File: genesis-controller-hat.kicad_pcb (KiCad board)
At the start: 2 copper layers, 65 x 56 mm, 7 parts, among them J1 GPIO, J2 DSUB-9_Socket_Vertical_P2.77x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, J3 DSUB-9_Socket_Vertical_P2.77x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

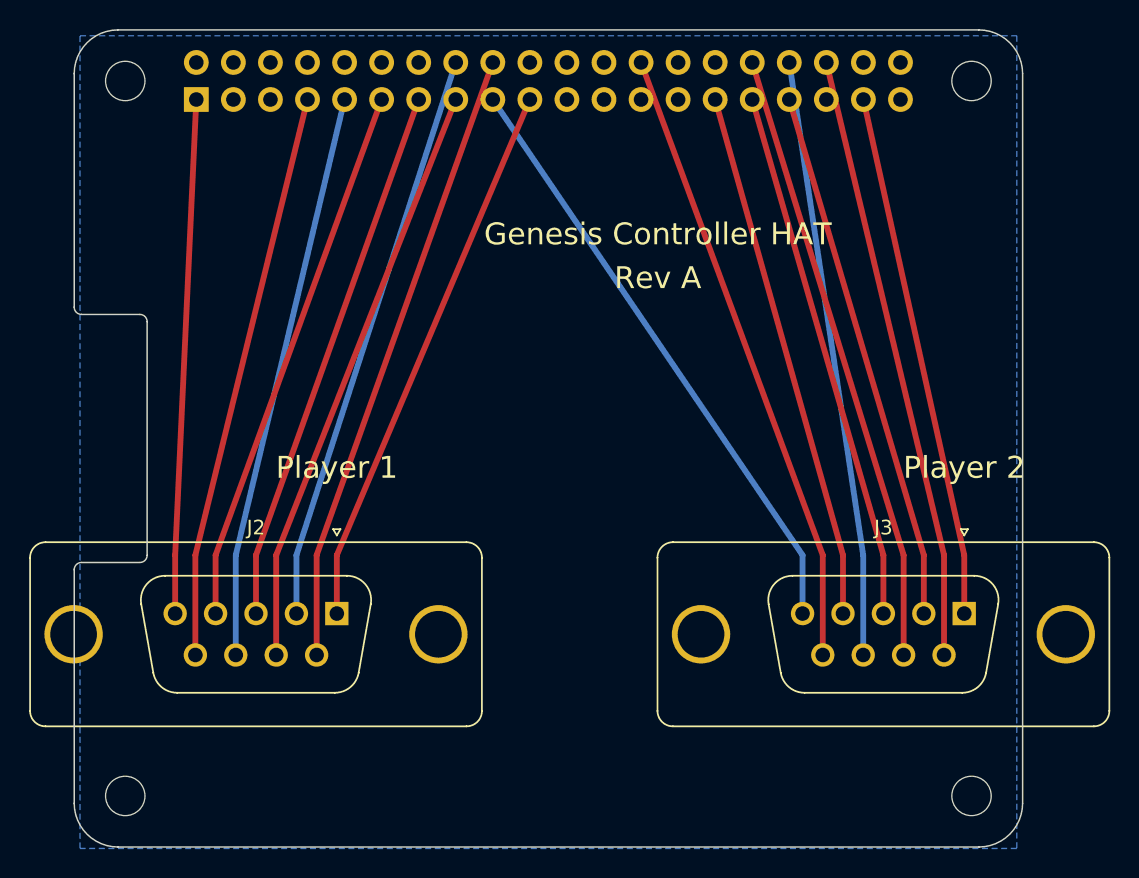
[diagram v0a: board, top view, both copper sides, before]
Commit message: Move J2/J3 inward so all 4 DSUB mounting holes sit fully on the board
J2's left mounting hole and J3's right mounting hole previously fell
partially/fully off the board edge (J2's left hole was bisected by the
edge; J3's right hole was entirely off-board). Moved J2 +3mm and J3 -6mm
so all 4 holes now sit fully on the board with ~1mm clearance to the edge,
leaving ~2mm clearance between the two connector shells. Re-routed both
connectors' traces to match (same breakout-and-diagonal technique as the
pin reassignment), still achieving 0 tracks_crossing / 0 hole_clearance /
0 copper_edge_clearance. Shifted the "Player 1"/"Player 2" silkscreen
labels to stay centered under their connectors.

DRC: 15 errors/7 warnings (was 15/6) — one more shorting_items and one
more silk_edge_clearance, both in the same pre-existing cosmetic/pad-graze
categories already documented as needing a manual GUI touch-up pass before
fabrication. ERC unaffected (0/0); schematic wiring is untouched by this
PCB-only change.

Co-Authored-By: Claude Sonnet 5 <noreply@anthropic.com>
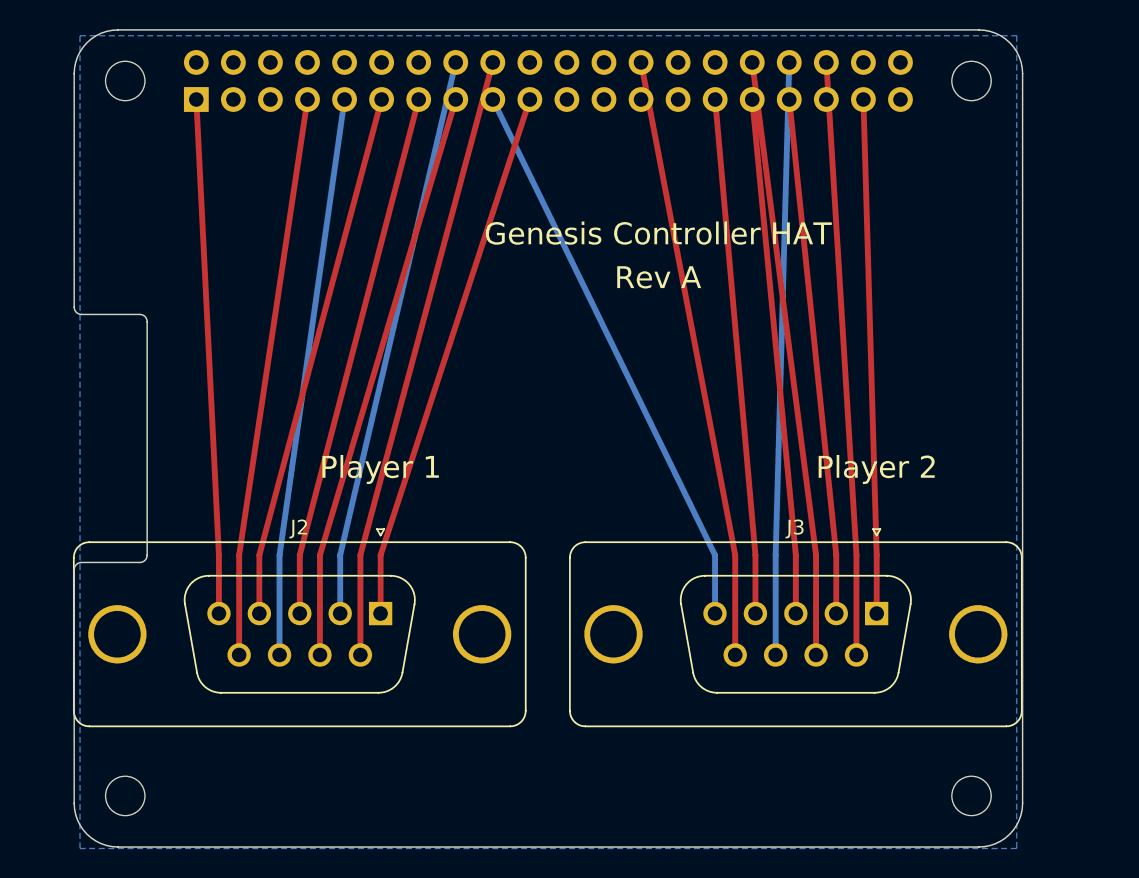
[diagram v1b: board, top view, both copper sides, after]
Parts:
- moved J3 6.00 mm to (155.0, 84.0)
- moved J2 3.00 mm to (121.0, 84.0)
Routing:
- net +3V3: track 77.0 -> 74.0 mm
- net /GPIO7/SPI0.CE1: track 42.8 -> 41.2 mm
- net /GPIO12/PWM0: track 42.2 -> 40.9 mm
- net /GPIO13/PWM1: track 36.6 -> 35.4 mm
- net /GPIO6: track 36.5 -> 35.4 mm
- net /GPIO5: track 36.4 -> 35.4 mm
- net /GPIO10/SPI0.MOSI: track 37.9 -> 36.9 mm
- net /GPIO22: track 40.4 -> 39.4 mm
- net GND: track 79.9 -> 79.0 mm
- net /GPIO17: track 37.2 -> 36.3 mm
- net /GPIO24: track 42.7 -> 41.8 mm
- net /GPIO16: track 41.6 -> 40.7 mm
- net /GPIO27: track 37.2 -> 36.3 mm
- net /GPIO23: track 39.5 -> 38.7 mm
- net /GPIO26: track 36.0 -> 35.2 mm
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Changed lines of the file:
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@@
 	(footprint "DSUB-9_Socket_Vertical_P2.77x2.84mm_MountingHoles"
 		(layer "F.Cu")
-		(at 118 84)
+		(at 121 84)
 		(descr "9-pin D-Sub connector, straight/vertical, THT-mount, socket (female), pitch 2.77x2.84mm, distance of mounting holes 25mm, see https://disti-assets.s3.amazonaws.com/tonar/files/datasheets/16730.pdf")
 		(tags "9-pin D-Sub connector straight vertical THT socket pitch 2.77x2.84mm mounting holes distance 25mm")
@@
 	(footprint "DSUB-9_Socket_Vertical_P2.77x2.84mm_MountingHoles"
 		(layer "F.Cu")
-		(at 161 84)
+		(at 155 84)
 		(descr "9-pin D-Sub connector, straight/vertical, THT-mount, socket (female), pitch 2.77x2.84mm, distance of mounting holes 25mm, see https://disti-assets.s3.amazonaws.com/tonar/files/datasheets/16730.pdf")
 		(tags "9-pin D-Sub connector straight vertical THT socket pitch 2.77x2.84mm mounting holes distance 25mm")
@@
 	)
 	(gr_text "Player 1"
-		(at 118 74 0)
+		(at 121.0 74 0)
 		(layer "F.SilkS")
 		(effects
@@
 	)
 	(gr_text "Player 2"
-		(at 161 74 0)
+		(at 155.0 74 0)
 		(layer "F.SilkS")
 		(effects
@@
 	)
 	(segment
-		(start 111.075 80)
-		(end 118.53 48.77)
+		(start 148.075 86.84)
+		(end 148.075 80)
 		(width 0.4)
 		(layer "B.Cu")
@@
 	)
 	(segment
-		(start 154.075 86.84)
-		(end 154.075 80)
+		(start 114.075 86.84)
+		(end 114.075 80)
 		(width 0.4)
 		(layer "B.Cu")
@@
 	)
 	(segment
-		(start 154.075 80)
+		(start 148.075 80)
 		(end 149.01 46.23)
 		(width 0.4)
@@
 	)
 	(segment
-		(start 111.075 86.84)
-		(end 111.075 80)
+		(start 114.075 80)
+		(end 118.53 48.77)
 		(width 0.4)
 		(layer "B.Cu")
@@
 	)
 	(segment
-		(start 108.305 86.84)
-		(end 108.305 80)
+		(start 111.305 80)
+		(end 115.99 48.77)
 		(width 0.4)
 		(layer "F.Cu")
@@
 	)
 	(segment
-		(start 108.305 80)
-		(end 115.99 48.77)
+		(start 111.305 86.84)
+		(end 111.305 80)
 		(width 0.4)
 		(layer "F.Cu")
@@
 	)
 	(segment
-		(start 109.69 80)
+		(start 112.69 80)
 		(end 121.07 48.77)
 		(width 0.4)
@@
 	)
 	(segment
-		(start 109.69 84)
-		(end 109.69 80)
+		(start 112.69 84)
+		(end 112.69 80)
 		(width 0.4)
 		(layer "F.Cu")
@@
 	)
 	(segment
-		(start 112.46 84)
-		(end 112.46 80)
+		(start 115.46 80)
+		(end 123.61 48.77)
 		(width 0.4)
 		(layer "F.Cu")
@@
 	)
 	(segment
-		(start 112.46 80)
-		(end 123.61 48.77)
+		(start 115.46 84)
+		(end 115.46 80)
 		(width 0.4)
 		(layer "F.Cu")
@@
 	)
 	(segment
-		(start 113.845 80)
+		(start 116.845 86.84)
+		(end 116.845 80)
+		(width 0.4)
+		(layer "F.Cu")
+		(net 10)
+	)
+	(segment
+		(start 116.845 80)
 		(end 126.15 48.77)
 		(width 0.4)
@@
 	)
 	(segment
-		(start 113.845 86.84)
-		(end 113.845 80)
-		(width 0.4)
-		(layer "F.Cu")
-		(net 10)
-	)
-	(segment
-		(start 115.23 80)
-		(end 126.15 46.23)
+		(start 118.23 84)
+		(end 118.23 80)
 		(width 0.4)
 		(layer "B.Cu")
@@
 	)
 	(segment
-		(start 115.23 84)
-		(end 115.23 80)
+		(start 118.23 80)
+		(end 126.15 46.23)
 		(width 0.4)
 		(layer "B.Cu")
@@
 	)
 	(segment
-		(start 116.615 86.84)
-		(end 116.615 80)
+		(start 119.615 86.84)
+		(end 119.615 80)
 		(width 0.4)
 		(layer "F.Cu")
@@
 	)
 	(segment
-		(start 116.615 80)
+		(start 119.615 80)
 		(end 128.69 46.23)
 		(width 0.4)
@@
 	)
 	(segment
-		(start 118 84)
-		(end 118 80)
+		(start 121 84)
+		(end 121 80)
 		(width 0.4)
 		(layer "F.Cu")
@@
 	)
 	(segment
-		(start 118 80)
+		(start 121 80)
 		(end 131.23 48.77)
 		(width 0.4)
@@
 	)
 	(segment
-		(start 151.305 80)
+		(start 145.305 80)
 		(end 138.85 46.23)
 		(width 0.4)
@@
 	)
 	(segment
-		(start 151.305 86.84)
-		(end 151.305 80)
+		(start 145.305 86.84)
+		(end 145.305 80)
 		(width 0.4)
 		(layer "F.Cu")
@@
 	)
 	(segment
-		(start 152.69 80)
+		(start 146.69 84)
+		(end 146.69 80)
+		(width 0.4)
+		(layer "F.Cu")
+		(net 21)
+	)
+	(segment
+		(start 146.69 80)
 		(end 143.93 48.77)
 		(width 0.4)
@@
 	)
 	(segment
-		(start 152.69 84)
-		(end 152.69 80)
-		(width 0.4)
-		(layer "F.Cu")
-		(net 21)
-	)
-	(segment
-		(start 155.46 80)
+		(start 149.46 80)
 		(end 146.47 48.77)
 		(width 0.4)
@@
 	)
 	(segment
-		(start 155.46 84)
-		(end 155.46 80)
+		(start 149.46 84)
+		(end 149.46 80)
 		(width 0.4)
 		(layer "F.Cu")
@@
 	)
 	(segment
-		(start 156.845 86.84)
-		(end 156.845 80)
+		(start 150.845 86.84)
+		(end 150.845 80)
 		(width 0.4)
 		(layer "F.Cu")
@@
 	)
 	(segment
-		(start 156.845 80)
+		(start 150.845 80)
 		(end 146.47 46.23)
 		(width 0.4)
@@
 	)
 	(segment
-		(start 158.23 80)
+		(start 152.23 80)
 		(end 149.01 48.77)
 		(width 0.4)
@@
 	)
 	(segment
-		(start 158.23 84)
-		(end 158.23 80)
+		(start 152.23 84)
+		(end 152.23 80)
 		(width 0.4)
 		(layer "F.Cu")
@@
 	)
 	(segment
-		(start 159.615 86.84)
-		(end 159.615 80)
+		(start 153.615 80)
+		(end 151.55 46.23)
 		(width 0.4)
 		(layer "F.Cu")
@@
 	)
 	(segment
-		(start 159.615 80)
-		(end 151.55 46.23)
+		(start 153.615 86.84)
+		(end 153.615 80)
 		(width 0.4)
 		(layer "F.Cu")
@@
 	)
 	(segment
-		(start 161 80)
+		(start 155 80)
 		(end 154.09 48.77)
 		(width 0.4)
@@
 	)
 	(segment
-		(start 161 84)
-		(end 161 80)
+		(start 155 84)
+		(end 155 80)
 		(width 0.4)
 		(layer "F.Cu")
@@
 	)
 	(segment
-		(start 106.92 80)
+		(start 109.92 84)
+		(end 109.92 80)
+		(width 0.4)
+		(layer "F.Cu")
+		(net 31)
+	)
+	(segment
+		(start 109.92 80)
 		(end 108.37 48.77)
 		(width 0.4)
@@
 	)
 	(segment
-		(start 106.92 84)
-		(end 106.92 80)
-		(width 0.4)
-		(layer "F.Cu")
-		(net 31)
-	)
-	(segment
-		(start 149.92 80)
-		(end 128.69 48.77)
+		(start 143.92 84)
+		(end 143.92 80)
 		(width 0.4)
 		(layer "B.Cu")
@@
 	)
 	(segment
-		(start 149.92 84)
-		(end 149.92 80)
+		(start 143.92 80)
+		(end 128.69 48.77)
 		(width 0.4)
 		(layer "B.Cu")
@@
 		(polygon
 			(pts
-				(xy 100.4 44.4) (xy 164.6 44.4) (xy 164.6 100.1) (xy 100.4 100.1)
-			)
-		)
+				(xy 100.4 44.4)
+				(xy 164.6 44.4)
+				(xy 164.6 100.1)
+				(xy 100.4 100.1)
+			)
+		)

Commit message: Switch J2/J3 to edge-mount DSUB footprint for edge-accessible cables
The previous DSUB-9_Socket_Vertical footprint has its mating opening
facing straight up, away from the board surface -- cables would plug in
from directly above the HAT, not from its edge. Switched to
DSUB-9_Socket_Horizontal_..._EdgePinOffset7.70mm_Housed_MountingHolesOffset9.12mm,
which hangs the connector's shell 9.12mm past the board's bottom edge so
cables plug in horizontally, console-style. Same pin/mounting-hole family
and X footprint as before, so the existing connector X-positions and
routing approach carry over; only the Y position and pin-to-J1 routing
were recomputed.

Known trade-off: the edge-mount connector's mounting bracket is 30.85mm
wide, and the board's corner mounting holes are only 58mm apart -- there is
no position that clears both each other and both corner holes
simultaneously. Prioritized J2/J3 not overlapping each other (the
alternative would make the parts unpopulatable) over full corner-hole
clearance, leaving 2 courtyards_overlap violations (J2 vs MH3, J3 vs MH4).
This is a real mechanical conflict to resolve before fabrication (documented
in README.md), not a routing artifact.

DRC: 17 errors/5 warnings (was 15/7) -- the 2 new courtyards_overlap plus
the pre-existing/cosmetic categories already documented. ERC unaffected
(0/0); schematic wiring is untouched by this PCB-only change.

Co-Authored-By: Claude Sonnet 5 <noreply@anthropic.com>
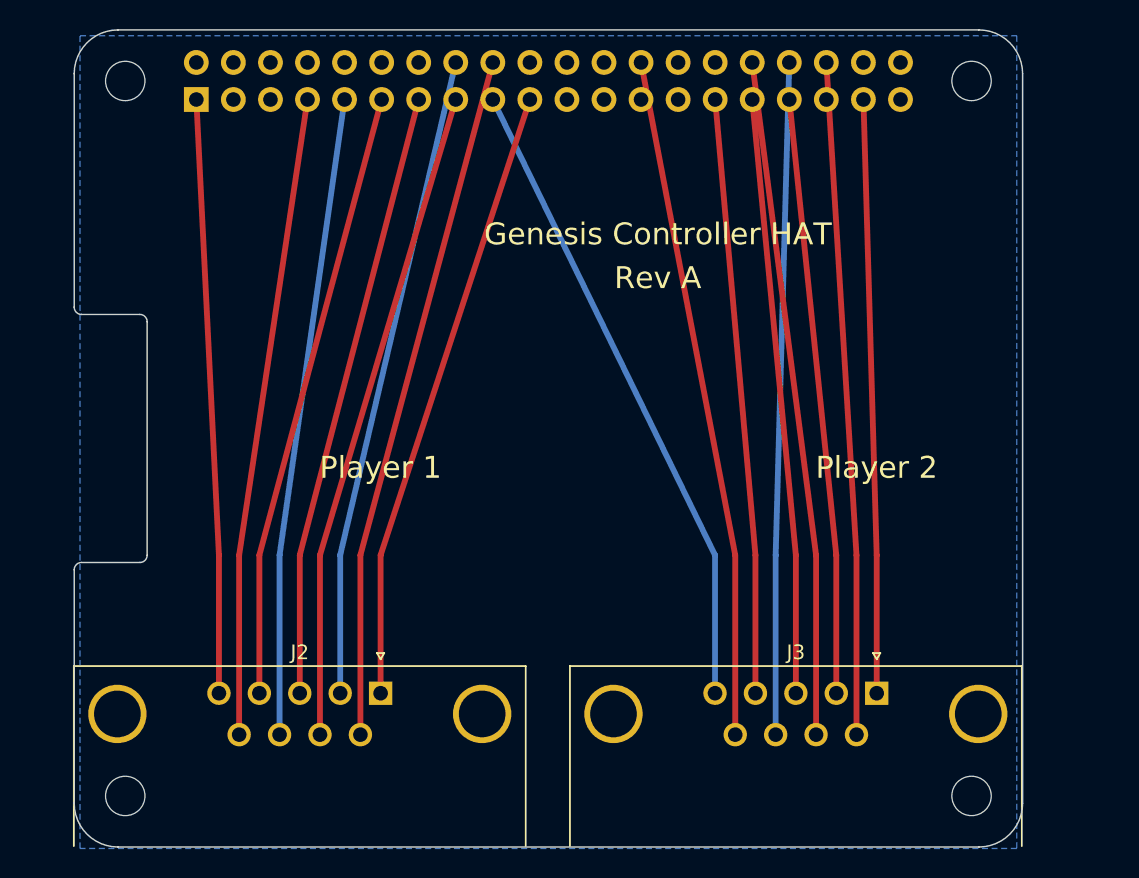
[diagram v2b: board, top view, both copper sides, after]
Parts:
- J2, J3: value DSUB-9_Socket_Vertical_P2.77x2.84mm_MountingHoles -> DSUB-9_Socket_Horizontal_P2.77x2.84mm_EdgePinOffset7.70mm_Housed_MountingHolesOffset9.12mm; footprint DSUB-9_Socket_Vertical_P2.77x2.84mm_MountingHoles -> DSUB-9_Socket_Horizontal_P2.77x2.84mm_EdgePinOffset7.70mm_Housed_MountingHolesOffset9.12mm
- moved J2 5.46 mm to (121.0, 89.5)
- moved J3 5.46 mm to (155.0, 89.5)
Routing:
- net GND: track 79.0 -> 89.9 mm
- net +3V3: track 74.0 -> 84.9 mm
- net /GPIO7/SPI0.CE1: track 41.2 -> 46.7 mm
- net /GPIO6: track 35.4 -> 40.8 mm
- net /GPIO5: track 35.4 -> 40.8 mm
- net /GPIO4/GPCLK0: track 38.4 -> 43.9 mm
- net /GPIO27: track 36.3 -> 41.7 mm
- net /GPIO26: track 35.2 -> 40.7 mm
- net /GPIO24: track 41.8 -> 47.3 mm
- net /GPIO23: track 38.7 -> 44.1 mm
- net /GPIO22: track 39.4 -> 44.9 mm
- net /GPIO17: track 36.3 -> 41.8 mm
- net /GPIO16: track 40.7 -> 46.1 mm
- net /GPIO13/PWM1: track 35.4 -> 40.9 mm
- net /GPIO12/PWM0: track 40.9 -> 46.4 mm
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
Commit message: Add Bare-Metal Genesis wordmark logo to board silkscreen
Replaces the plain "Genesis Controller HAT" title text with the wordmark
logo from design_files/Bare-metal Sega Genesis-handoff.zip
(project/kicad/bmg-logo-wordmark.svg). The source SVG is entirely
axis-aligned rects (pixel-art style), so it converts directly to 153
filled gr_rect silkscreen shapes on F.Silkscreen at 1:1 fidelity, no
tracing/vectorization needed. Sized 48mm wide (~14mm tall) and centered in
the open area between J1 and the DB9 connectors; "Rev A" nudged down
slightly to stay clear of it.

ERC/DRC unaffected (silkscreen doesn't need clearance from the copper
traces it visually sits over). Added design_files/ to the repo for
provenance.

Co-Authored-By: Claude Sonnet 5 <noreply@anthropic.com>
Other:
- board text removed: "Genesis Controller HAT"

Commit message: Add back "Controller HAT" text, in line with "Rev A"
Restores the "Controller HAT" part of the old title text (dropped when the
wordmark logo replaced "Genesis Controller HAT"), placed on the same line
as "Rev A" just below the logo. Both centered as a pair under the logo,
clear of the logo above and the Player 1/Player 2 labels below.

ERC/DRC unaffected (0 errors/2 warnings, 17/5 -- same as before).

Co-Authored-By: Claude Sonnet 5 <noreply@anthropic.com>
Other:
- board text added: "Controller HAT"
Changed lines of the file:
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@@
+		)
+	)
+	(gr_text "Controller HAT"
+		(at 127.69 70.5 0)
+		(layer "F.SilkS")
+		(effects
+			(font
+				(size 1.5 1.5)
+			)
 		)
 	)
 	(gr_text "Rev A"
-		(at 140 70.5 0)
+		(at 143.27 70.5 0)
 		(layer "F.SilkS")
 		(effects

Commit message: Add repo URL and build date to back silkscreen
Front silkscreen was already full (logo, title, port labels), so the repo
URL (github.com/mjaydedecker/Bare-Metal-Sega-Genesis-Hat) and a "Jul 2026"
build date go on B.Silkscreen instead. Set SetMirrored(True) on both --
without it, back-layer text renders backwards once the board is physically
flipped over (confirmed by rendering --side bottom before and after).

ERC/DRC unaffected (0 errors/2 warnings, 17/5 -- same as before).

Co-Authored-By: Claude Sonnet 5 <noreply@anthropic.com>
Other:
- board text added: "Jul 2026"
- board text added: "github.com/mjaydedecker/Bare-Metal-Sega-Genesis-Hat"
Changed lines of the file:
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@@
+		)
+	)
+	(gr_text "github.com/mjaydedecker/Bare-Metal-Sega-Genesis-Hat"
+		(at 132.5 60 0)
+		(layer "B.SilkS")
+		(effects
+			(font
+				(size 1 1)
+			)
+			(justify mirror)
+		)
+	)
+	(gr_text "Jul 2026"
+		(at 132.5 65 0)
+		(layer "B.SilkS")
+		(effects
+			(font
+				(size 1.5 1.5)
+			)
+			(justify mirror)
 		)
 	)
